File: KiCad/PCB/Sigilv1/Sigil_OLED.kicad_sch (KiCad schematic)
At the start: 17 parts, among them J2 INLAND 1.3" OLED HEADER (7-PI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, J3 BUZZER 2-PIN HEADER, J5 STATUS RING CABLE (JST-XH 3), J6 FRONT LIGHT CABLE (JST-XH 3), SW1 UP (GPIO25, J11), SW2 DOWN (GPIO27, J9), SW3 LEFT (GPIO19, A12), SW4 RIGHT (GPIO21, A14), SW5 SELECT (GPIO32, J13), U1 REMOVABLE ESP32 DEVKIT / 2 x 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, U2 74AHCT1G125, U3 74AHCT1G125

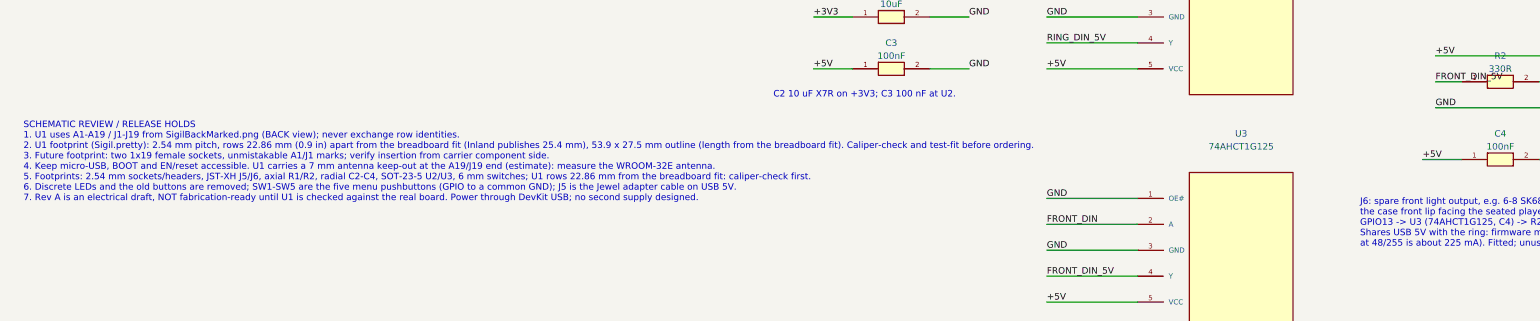
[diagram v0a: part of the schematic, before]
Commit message: Sigil E-ink PCB: measured DevKit footprint, routed board, fab outputs
- U1 footprint rows 22.225 mm (7/8 in) apart per owner measurement,
  25.4 x 53.975 mm outline; renamed ESP32_DevKit_38_Socket_Row22.225mm.
- Antenna keep-out narrowed to the measured antenna (6.35 x 19.05 mm)
  so the pin rows stay routable.
- Board top edge moved up 0.5 mm to clear silkscreen.
- Routed with Freerouting v2.4.1 plus a hand-placed BUZZER track; GND
  pours on both layers with solid pad connections. KiCad 10.0.6 DRC:
  0 violations, 0 unconnected, 0 schematic parity issues.
- Added BOM CSV, Gerber/drill zip and position CSV under fab/.
- Not fabrication-verified: U1 row spacing still needs a test-fit.

Co-Authored-By: Claude Opus 5.5 <noreply@anthropic.com>
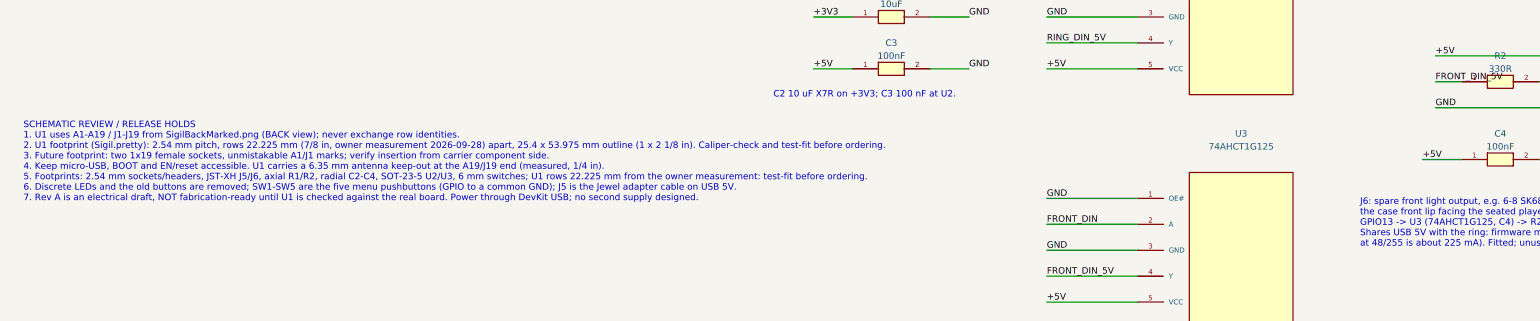
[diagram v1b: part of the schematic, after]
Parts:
- U1: footprint Sigil:ESP32_DevKit_38_Socket_Row22.86mm -> Sigil:ESP32_DevKit_38_Socket_Row22.225mm
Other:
- note added: "SCHEMATIC REVIEW / RELEASE HOLDS 1. U1 uses A1-A19 / J1-J19 from SigilBackMarked.png (BACK view); never exchange row identities. 2. U1 footprint (Sigil.pretty): 2.54 mm pitch, rows 22.225 mm (7/8 in, owner measurement 2026-09-28) apart, 25.4 x 53.975 mm outline (1 x 2 1/8 in). Caliper-check and test-fit before ordering. 3. Future footprint: two 1x19 female sockets, unmistakable A1/J1 marks; verif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"
- note removed: "SCHEMATIC REVIEW / RELEASE HOLDS 1. U1 uses A1-A19 / J1-J19 from SigilBackMarked.png (BACK view); never exchange row identities. 2. U1 footprint (Sigil.pretty): 2.54 mm pitch, rows 22.86 mm (0.9 in) apart from the breadboard fit (Inland publishes 25.4 mm), 53.9 x 27.5 mm outline (length from the breadboard fit). Caliper-check and test-fit before ordering. 3. Future footprint: two 1x19 female sock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"
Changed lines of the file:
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@@
 		)
 	)
-	(text "SCHEMATIC REVIEW / RELEASE HOLDS\n1. U1 uses A1-A19 / J1-J19 from SigilBackMarked.png (BACK view); never exchange row identities.\n2. U1 footprint (Sigil.pretty): 2.54 mm pitch, rows 22.86 mm (0.9 in) apart from the breadboard fit (Inland publishes 25.4 mm), 53.9 x 27.5 mm outline (length from the breadboard fit). Caliper-check and test-fit before ordering.\n3. Future footprint: two 1x19 female sockets, unmistakable A1/J1 marks; verify insertion from carrier component side.\n4. Keep micro-USB, BOOT and EN/reset accessible. U1 carries a 7 mm antenna keep-out at the A19/J19 end (estimate): measure the WROOM-32E antenna.\n5. Footprints: 2.54 mm sockets/headers, JST-XH J5/J6, axial R1/R2, radial C2-C4, SOT-23-5 U2/U3, 6 mm switches; U1 rows 22.86 mm from the breadboard fit: caliper-check first.\n6. Discrete LEDs and the old buttons are removed; SW1-SW5 are the five menu pushbuttons (GPIO to a common GND); J5 is the Jewel adapter cable on USB 5V.\n7. Rev A is an electrical draft, NOT fabrication-ready until U1 is checked against the real board. Power through DevKit USB; no second supply designed."
+	(text "SCHEMATIC REVIEW / RELEASE HOLDS\n1. U1 uses A1-A19 / J1-J19 from SigilBackMarked.png (BACK view); never exchange row identities.\n2. U1 footprint (Sigil.pretty): 2.54 mm pitch, rows 22.225 mm (7/8 in, owner measurement 2026-09-28) apart, 25.4 x 53.975 mm outline (1 x 2 1/8 in). Caliper-check and test-fit before ordering.\n3. Future footprint: two 1x19 female sockets, unmistakable A1/J1 marks; verify insertion from carrier component side.\n4. Keep micro-USB, BOOT and EN/reset accessible. U1 carries a 6.35 mm antenna keep-out at the A19/J19 end (measured, 1/4 in).\n5. Footprints: 2.54 mm sockets/headers, JST-XH J5/J6, axial R1/R2, radial C2-C4, SOT-23-5 U2/U3, 6 mm switches; U1 rows 22.225 mm from the owner measurement: test-fit before ordering.\n6. Discrete LEDs and the old buttons are removed; SW1-SW5 are the five menu pushbuttons (GPIO to a common GND); J5 is the Jewel adapter cable on USB 5V.\n7. Rev A is an electrical draft, NOT fabrication-ready until U1 is checked against the real board. Power through DevKit USB; no second supply designed."
 		(exclude_from_sim no)
 		(at 28 211 0)
@@
 			)
 		)
-		(property "Footprint" "Sigil:ESP32_DevKit_38_Socket_Row22.86mm"
+		(property "Footprint" "Sigil:ESP32_DevKit_38_Socket_Row22.225mm"
 			(at 88.9 101.6 0)
 			(hide yes)

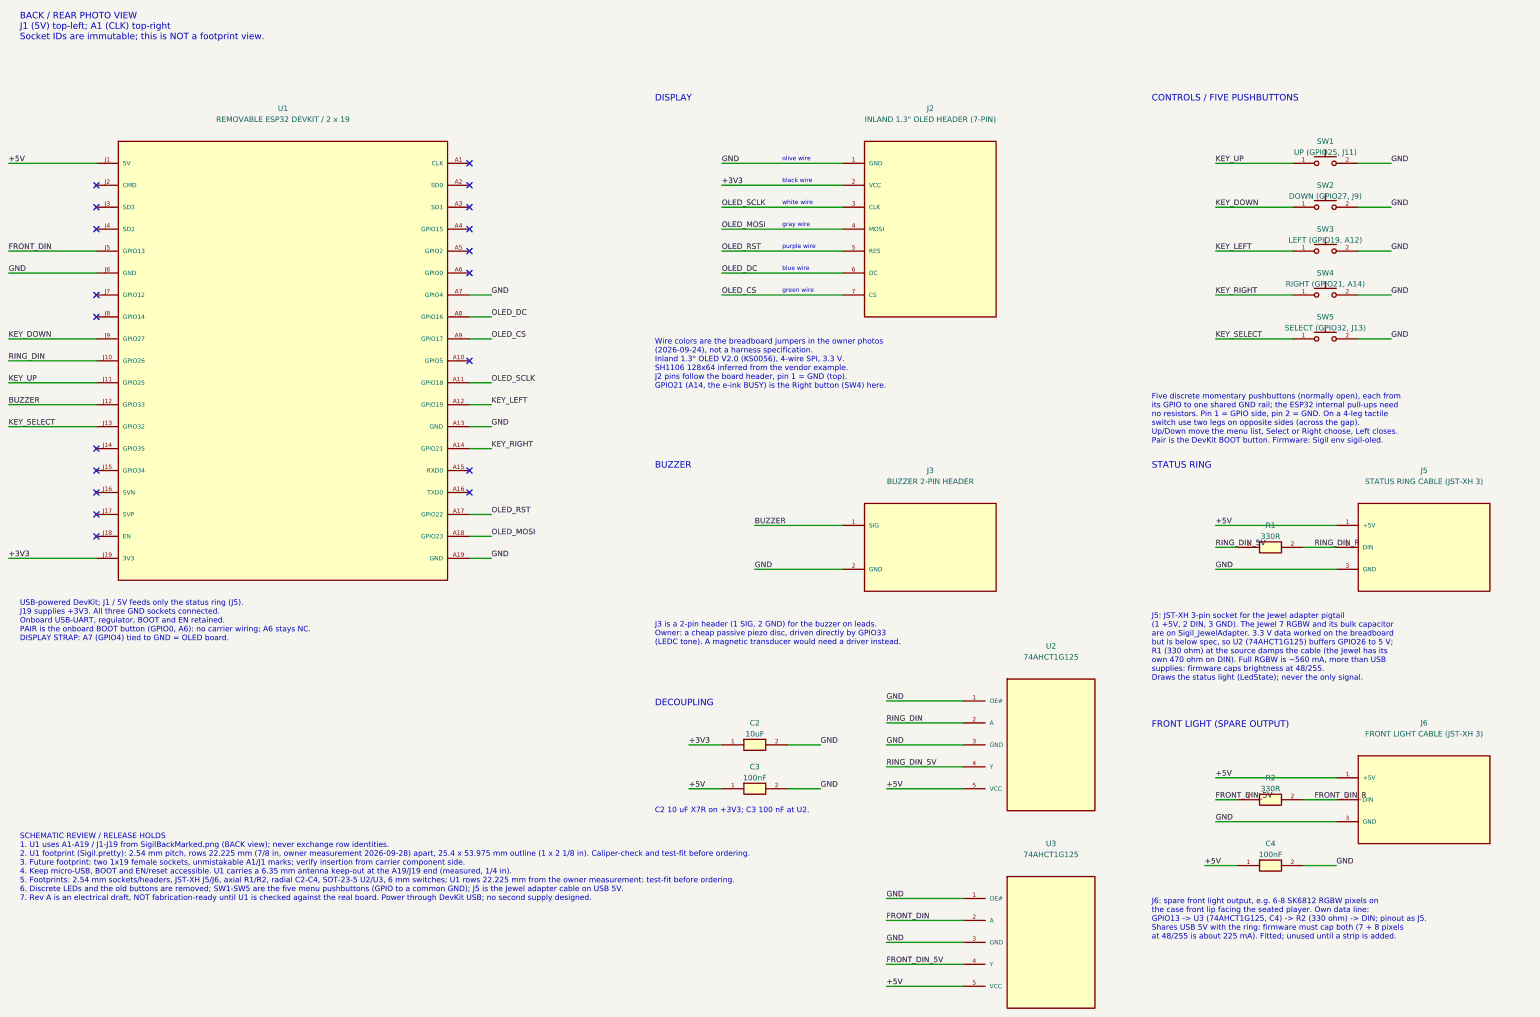
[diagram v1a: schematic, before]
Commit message: KiCad: Sigil_OLED draws the joystick J4 like the E-ink; SW1-SW5 removed
The OLED Sigil uses the same thumbstick on the same GPIOs (34/35/32) since
2026-10-01, so build_schematic.py gives it J4 and drops the pushbutton
symbol, footprint and drawing; verify_schematic.py checks the joystick rows
on both drafts. KiCad 10 CLI ERC: 0 violations on all three schematics;
verify_schematic.py passes; E-ink PCB DRC and schematic parity still clean
(its schematic changed only in note text). README, hardware reference and
STAGED_CHANGES updated.

Co-Authored-By: Claude Opus 5.5 <noreply@anthropic.com>
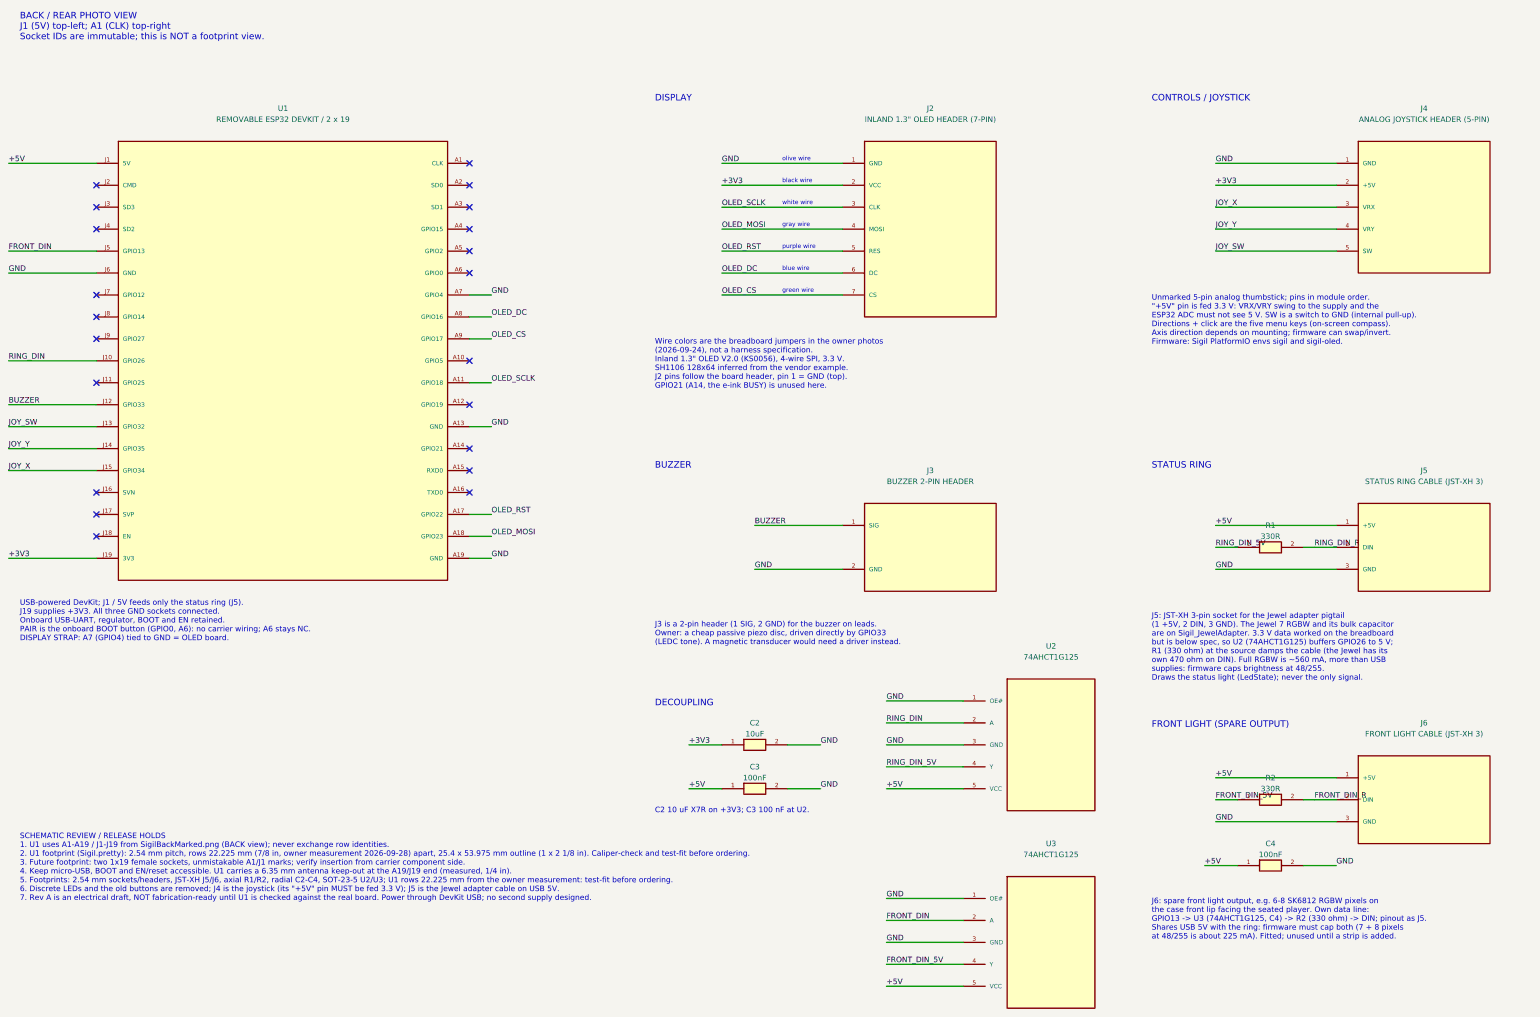
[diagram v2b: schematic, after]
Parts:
- removed SW1: UP (GPIO25, J11), Button_Switch_THT:SW_PUSH_6mm, symbol Sigil:Pushbutton_SPST_NO
- removed SW2: DOWN (GPIO27, J9), Button_Switch_THT:SW_PUSH_6mm, symbol Sigil:Pushbutton_SPST_NO
- removed SW3: LEFT (GPIO19, A12), Button_Switch_THT:SW_PUSH_6mm, symbol Sigil:Pushbutton_SPST_NO
- removed SW4: RIGHT (GPIO21, A14), Button_Switch_THT:SW_PUSH_6mm, symbol Sigil:Pushbutton_SPST_NO
- removed SW5: SELECT (GPIO32, J13), Button_Switch_THT:SW_PUSH_6mm, symbol Sigil:Pushbutton_SPST_NO
- added J4: ANALOG JOYSTICK HEADER (5-PIN), Connector_JST:JST_XH_B5B-XH-A_1x05_P2.50mm_Vertical, symbol Sigil:Joystick_Module_Header
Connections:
- net +3V3: now also J4.2 (+5V)
- net GND: now also J4.1 (GND)
- net JOY_Y: now reaches U1.J14 (GPIO35)
- net JOY_Y: now also J4.4 (VRY)
- net JOY_X: now reaches U1.J15 (GPIO34)
- net JOY_X: now also J4.3 (VRX)
- net KEY_DOWN: no longer names the net of U1.J9 (GPIO27)
- net KEY_LEFT: no longer names the net of U1.A12 (GPIO19)
- net KEY_RIGHT: no longer names the net of U1.A14 (GPIO21)
- net KEY_SELECT renamed JOY_SW
- net JOY_SW: now also J4.5 (SW)
- net KEY_UP: no longer names the net of U1.J11 (GPIO25)
- no-connect marks 19 -> 21
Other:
- note added: "CONTROLS / JOYSTICK"
- note added: "Unmarked 5-pin analog thumbstick; pins in module order. "+5V" pin is fed 3.3 V: VRX/VRY swing to the supply and the ESP32 ADC must not see 5 V. SW is a switch to GND (internal pull-up). Directions + click are the five menu keys (on-screen compass). Axis direction depends on mounting; firmware can swap/invert. Firmware: Sigil PlatformIO envs sigil and sigil-oled."
- note added: "Wire colors are the breadboard jumpers in the owner photos (2026-09-24), not a harness specification. Inland 1.3" OLED V2.0 (KS0056), 4-wire SPI, 3.3 V. SH1106 128x64 inferred from the vendor example. J2 pins follow the board header, pin 1 = GND (top). GPIO21 (A14, the e-ink BUSY) is unused here."
- note removed: "CONTROLS / FIVE PUSHBUTTONS"
- note removed: "Five discrete momentary pushbuttons (normally open), each from its GPIO to one shared GND rail; the ESP32 internal pull-ups need no resistors. Pin 1 = GPIO side, pin 2 = GND. On a 4-leg tactile switch use two legs on opposite sides (across the gap). Up/Down move the menu list, Select or Right choose, Left closes. Pair is the DevKit BOOT button. Firmware: Sigil env sigil-oled."
- note removed: "Wire colors are the breadboard jumpers in the owner photos (2026-09-24), not a harness specification. Inland 1.3" OLED V2.0 (KS0056), 4-wire SPI, 3.3 V. SH1106 128x64 inferred from the vendor example. J2 pins follow the board header, pin 1 = GND (top). GPIO21 (A14, the e-ink BUSY) is the Right button (SW4) here."
